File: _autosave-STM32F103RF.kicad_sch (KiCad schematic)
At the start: 14 parts, among them J1 USB_C_Receptacle_USB2.0, U1 SPX3819M5-L-3-3

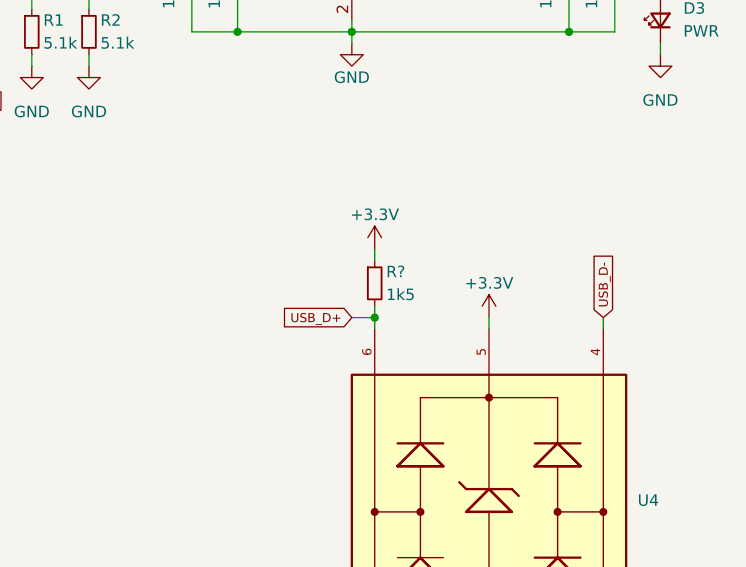
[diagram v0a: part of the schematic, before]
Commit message: added proper ESD Protection for USB
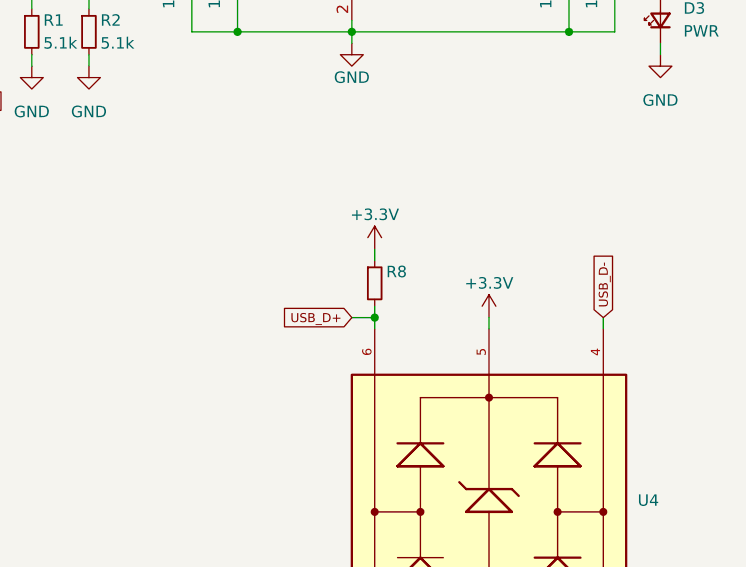
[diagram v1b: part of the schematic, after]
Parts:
- R8: renamed from R?; value 1k5 -> (none); footprint Resistor_SMD:R_0603_1608Metric_Pad0.98x0.95mm_HandSolder -> (none)
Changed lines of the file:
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@@
   (symbol (lib_id "Device:R_Small") (at 165.1 105.41 0) (unit 1)
     (in_bom yes) (on_board yes)
-    (property "Reference" "R?" (id 0) (at 166.37 104.14 0)
-      (effects (font (size 1.27 1.27)) (justify left))
-    )
-    (property "Value" "1k5" (id 1) (at 166.37 106.68 0)
-      (effects (font (size 1.27 1.27)) (justify left))
-    )
-    (property "Footprint" "Resistor_SMD:R_0603_1608Metric_Pad0.98x0.95mm_HandSolder" (id 2) (at 165.1 105.41 0)
+    (property "Reference" "R8" (id 0) (at 166.37 104.14 0)
+      (effects (font (size 1.27 1.27)) (justify left))
+    )
+    (property "Value" "" (id 1) (at 166.37 106.68 0)
+      (effects (font (size 1.27 1.27)) (justify left))
+    )
+    (property "Footprint" "" (id 2) (at 165.1 105.41 0)
       (effects (font (size 1.27 1.27)) hide)
     )
@@
   (symbol (lib_id "power:+3.3V") (at 165.1 101.6 0) (unit 1)
     (in_bom yes) (on_board yes)
-    (property "Reference" "#PWR?" (id 0) (at 165.1 105.41 0)
+    (property "Reference" "#PWR0123" (id 0) (at 165.1 105.41 0)
       (effects (font (size 1.27 1.27)) hide)
     )
@@
       (reference "#PWR0122") (unit 1) (value "GND") (footprint "")
     )
+    (path "/e254c0e8-f02b-4e48-af06-527a002e8786"
+      (reference "#PWR0123") (unit 1) (value "+3.3V") (footprint "")
+    )
     (path "/3b596506-65bf-4a2a-90c0-c8e397dd346e/e3b920fe-b68f-42e9-9323-4e14aea9e91f"
       (reference "#PWR0124") (unit 1) (value "GND") (footprint "")
@@
       (reference "#PWR0143") (unit 1) (value "GND") (footprint "")
     )
-    (path "/e254c0e8-f02b-4e48-af06-527a002e8786"
-      (reference "#PWR?") (unit 1) (value "+3.3V") (footprint "")
-    )
     (path "/2db55799-9633-47c9-893c-575bc0ed35bb"
       (reference "C1") (unit 1) (value "10u") (footprint "Capacitor_SMD:C_0603_1608Metric_Pad1.08x0.95mm_HandSolder")
@@
       (reference "R7") (unit 1) (value "300") (footprint "Resistor_SMD:R_0603_1608Metric_Pad0.98x0.95mm_HandSolder")
     )
+    (path "/bb3724a8-4fc1-4f9d-b24d-1fd2f0be8d2f"
+      (reference "R8") (unit 1) (value "1k5") (footprint "Resistor_SMD:R_0603_1608Metric_Pad0.98x0.95mm_HandSolder")
+    )
     (path "/3b596506-65bf-4a2a-90c0-c8e397dd346e/cba8547d-fcd7-4a73-864a-fcec269f61d5"
       (reference "R9") (unit 1) (value "10k") (footprint "Resistor_SMD:R_0603_1608Metric_Pad0.98x0.95mm_HandSolder")
@@
       (reference "R11") (unit 1) (value "1M") (footprint "Resistor_SMD:R_0603_1608Metric_Pad0.98x0.95mm_HandSolder")
     )
-    (path "/bb3724a8-4fc1-4f9d-b24d-1fd2f0be8d2f"
-      (reference "R?") (unit 1) (value "1k5") (footprint "Resistor_SMD:R_0603_1608Metric_Pad0.98x0.95mm_HandSolder")
-    )
     (path "/c6b070fb-230d-42f9-b182-7a55fca635e2"
